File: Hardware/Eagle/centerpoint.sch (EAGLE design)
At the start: 5 parts, among them M1 ARDUINO-NANO-3.0

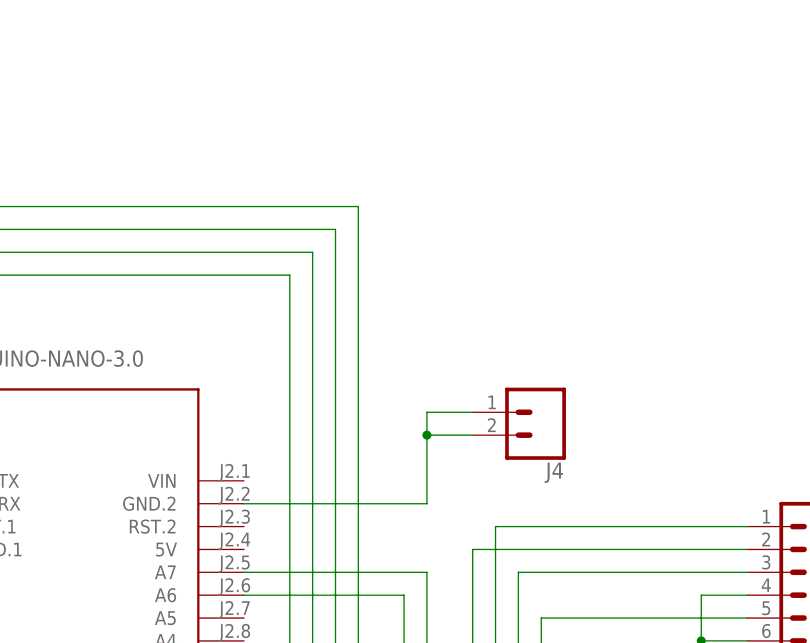
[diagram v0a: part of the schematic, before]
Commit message: added power switch and screw terminal for battery (VIN)
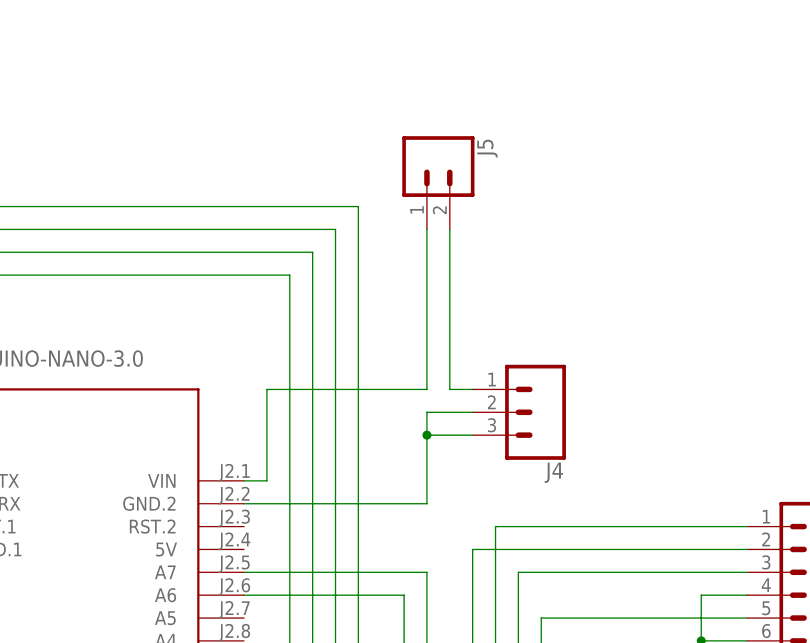
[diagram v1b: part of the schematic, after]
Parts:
- added J5: (no value), SparkFun-Connectors:CONN_023.5MM
- J4: device SparkFun-Connectors:CONN_023.5MM -> SparkFun-Connectors:CONN_03-SCREW-5MM
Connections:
- new net N$21: J5.1, M1.VIN
- new net N$22: J4.1, J5.2
- net N$20: now also J4.3; no longer J4.1
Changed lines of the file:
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@@
 <part name="J2" library="SparkFun-Connectors" deviceset="CONN_13" device="" override_package3d_urn="urn:adsk.eagle:package:30895386/5" override_package_urn="urn:adsk.eagle:footprint:30895387/1"/>
 <part name="J3" library="SparkFun-Connectors" deviceset="CONN_04" device="PTH" override_package3d_urn="urn:adsk.eagle:package:30895441/4" override_package_urn="urn:adsk.eagle:footprint:30895442/1"/>
-<part name="J4" library="SparkFun-Connectors" library_urn="urn:adsk.eagle:library:513" deviceset="CONN_02" device="3.5MM" package3d_urn="urn:adsk.eagle:package:38050/1" override_package3d_urn="urn:adsk.eagle:package:30895519/3" override_package_urn="urn:adsk.eagle:footprint:37656/1"/>
+<part name="J4" library="SparkFun-Connectors" library_urn="urn:adsk.eagle:library:513" deviceset="CONN_03" device="-SCREW-5MM" package3d_urn="urn:adsk.eagle:package:38070/1" override_package3d_urn="urn:adsk.eagle:package:30895519/6" override_package_urn="urn:adsk.eagle:footprint:30937717/1"/>
+<part name="J5" library="SparkFun-Connectors" library_urn="urn:adsk.eagle:library:513" deviceset="CONN_02" device="3.5MM" package3d_urn="urn:adsk.eagle:package:38050/1" override_package3d_urn="urn:adsk.eagle:package:30937787/2" override_package_urn="urn:adsk.eagle:footprint:37656/1"/>
 </parts>
 <sheets>
@@
 <attribute name="NAME" x="167.64" y="-30.988" size="1.778" layer="95" font="vector" rot="R180"/>
 </instance>
-<instance part="J4" gate="G$1" x="167.64" y="58.42" smashed="yes" rot="R180">
+<instance part="J4" gate="J$1" x="167.64" y="58.42" smashed="yes" rot="R180">
 <attribute name="VALUE" x="170.18" y="63.246" size="1.778" layer="96" font="vector" rot="R180"/>
 <attribute name="NAME" x="170.18" y="52.832" size="1.778" layer="95" font="vector" rot="R180"/>
+</instance>
+<instance part="J5" gate="G$1" x="154.94" y="86.36" smashed="yes" rot="R270">
+<attribute name="VALUE" x="150.114" y="88.9" size="1.778" layer="96" font="vector" rot="R270"/>
+<attribute name="NAME" x="160.528" y="88.9" size="1.778" layer="95" font="vector" rot="R270"/>
 </instance>
 </instances>
@@
 <wire x1="134.62" y1="48.26" x2="154.94" y2="48.26" width="0.1524" layer="91"/>
 <wire x1="154.94" y1="48.26" x2="154.94" y2="55.88" width="0.1524" layer="91"/>
-<pinref part="J4" gate="G$1" pin="1"/>
+<pinref part="J4" gate="J$1" pin="2"/>
 <wire x1="154.94" y1="55.88" x2="154.94" y2="58.42" width="0.1524" layer="91"/>
 <wire x1="154.94" y1="58.42" x2="160.02" y2="58.42" width="0.1524" layer="91"/>
-<pinref part="J4" gate="G$1" pin="2"/>
+<pinref part="J4" gate="J$1" pin="3"/>
 <wire x1="160.02" y1="55.88" x2="154.94" y2="55.88" width="0.1524" layer="91"/>
 <junction x="154.94" y="55.88"/>
@@
 </segment>
 </net>
+<net name="N$21" class="0">
+<segment>
+<pinref part="M1" gate="G$1" pin="VIN"/>
+<wire x1="134.62" y1="50.8" x2="137.16" y2="50.8" width="0.1524" layer="91"/>
+<wire x1="137.16" y1="50.8" x2="137.16" y2="60.96" width="0.1524" layer="91"/>
+<wire x1="137.16" y1="60.96" x2="154.94" y2="60.96" width="0.1524" layer="91"/>
+<pinref part="J5" gate="G$1" pin="1"/>
+<wire x1="154.94" y1="60.96" x2="154.94" y2="78.74" width="0.1524" layer="91"/>
+</segment>
+</net>
+<net name="N$22" class="0">
+<segment>
+<pinref part="J5" gate="G$1" pin="2"/>
+<wire x1="157.48" y1="78.74" x2="157.48" y2="60.96" width="0.1524" layer="91"/>
+<pinref part="J4" gate="J$1" pin="1"/>
+<wire x1="157.48" y1="60.96" x2="160.02" y2="60.96" width="0.1524" layer="91"/>
+</segment>
+</net>
